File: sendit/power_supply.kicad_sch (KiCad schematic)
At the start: 1 part, among them U9 TPS61040DBV

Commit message: bigger update
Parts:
- added C22: C_Small, symbol Device:C_Small
- added C23: 22pF, symbol Device:C_Small
- added C24: 1uF, symbol Device:C_Small
- added D17: MBR0530, Diode_SMD:D_SOD-123, symbol Diode:MBR0530
- added L1: 10uH, symbol Device:L
- added R68: 1.87M, symbol Device:R_Small_US
- added R69: 100k, symbol Device:R_Small_US
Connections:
- net at U9.1 (SW): now also D17.2 (A), L1.2
- net GND: now reaches U9.2 (GND)
- net GND: now also C22.2, C24.2, R69.2
- net at U9.3 (FB): now also C23.2, R68.2, R69.1
- net +5V: now reaches U9.4 (EN)
- net +5V: now also U9.5 (VIN), C22.1, L1.1
- new net +24V: C23.1, C24.1, D17.1 (K), R68.1

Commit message: layout work.
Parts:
- C10: renamed from C22; value C_Small -> 10uF; footprint (none) -> Capacitor_SMD:C_0603_1608Metric
- C11: renamed from C23; footprint (none) -> Capacitor_SMD:C_0603_1608Metric
- C12: renamed from C24; footprint (none) -> Capacitor_SMD:C_1206_3216Metric
- L1: footprint (none) -> Inductor_SMD:L_Ferrocore_DLG-0403; LCSC (none) -> C2929419
- R43: renamed from R68; footprint (none) -> Resistor_SMD:R_0603_1608Metric
- R44: renamed from R69; footprint (none) -> Resistor_SMD:R_0603_1608Metric
- renumbered D17 to D6, U9 to U4
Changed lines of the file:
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@@
 		(dnp no)
 		(fields_autoplaced yes)
-		(property "Reference" "#PWR0113"
+		(property "Reference" "#PWR067"
 			(at 129.54 121.92 0)
 			(effects
@@
 			(project "sendit"
 				(path "/a355e4d0-2918-44fc-be8d-2503b84c6d6c/336de2d2-126c-456c-9b27-fa88f8fd80ba"
-					(reference "#PWR0113")
+					(reference "#PWR067")
 					(unit 1)
 				)
@@
 		(dnp no)
 		(fields_autoplaced yes)
-		(property "Reference" "C24"
+		(property "Reference" "C12"
 			(at 182.88 90.1762 0)
 			(effects
@@
 			)
 		)
-		(property "Footprint" ""
+		(property "Footprint" "Capacitor_SMD:C_1206_3216Metric"
 			(at 180.34 91.44 0)
 			(effects
@@
 			(project "sendit"
 				(path "/a355e4d0-2918-44fc-be8d-2503b84c6d6c/336de2d2-126c-456c-9b27-fa88f8fd80ba"
-					(reference "C24")
+					(reference "C12")
 					(unit 1)
 				)
@@
 		(dnp no)
 		(fields_autoplaced yes)
-		(property "Reference" "R69"
+		(property "Reference" "R44"
 			(at 157.48 102.8699 0)
 			(effects
@@
 			)
 		)
-		(property "Footprint" ""
+		(property "Footprint" "Resistor_SMD:R_0603_1608Metric"
 			(at 154.94 104.14 0)
 			(effects
@@
 			(project "sendit"
 				(path "/a355e4d0-2918-44fc-be8d-2503b84c6d6c/336de2d2-126c-456c-9b27-fa88f8fd80ba"
-					(reference "R69")
+					(reference "R44")
 					(unit 1)
 				)
@@
 		(dnp no)
 		(fields_autoplaced yes)
-		(property "Reference" "U9"
+		(property "Reference" "U4"
 			(at 129.54 87.63 0)
 			(effects
@@
 			(project ""
 				(path "/a355e4d0-2918-44fc-be8d-2503b84c6d6c/336de2d2-126c-456c-9b27-fa88f8fd80ba"
-					(reference "U9")
+					(reference "U4")
 					(unit 1)
 				)
@@
 		(dnp no)
 		(fields_autoplaced yes)
-		(property "Reference" "C23"
+		(property "Reference" "C11"
 			(at 170.18 90.1762 0)
 			(effects
@@
 			)
 		)
-		(property "Footprint" ""
+		(property "Footprint" "Capacitor_SMD:C_0603_1608Metric"
 			(at 167.64 91.44 0)
 			(effects
@@
 			(project "sendit"
 				(path "/a355e4d0-2918-44fc-be8d-2503b84c6d6c/336de2d2-126c-456c-9b27-fa88f8fd80ba"
-					(reference "C23")
+					(reference "C11")
 					(unit 1)
 				)
@@
 			)
 		)
-		(property "Footprint" ""
+		(property "Footprint" "Inductor_SMD:L_Ferrocore_DLG-0403"
 			(at 129.54 82.55 0)
 			(effects
@@
 			)
 		)
+		(property "LCSC" "C2929419"
+			(at 129.54 82.55 90)
+			(effects
+				(font
+					(size 1.27 1.27)
+				)
+				(hide yes)
+			)
+		)
 		(pin "1"
 		)
@@
 		(dnp no)
 		(fields_autoplaced yes)
-		(property "Reference" "R68"
+		(property "Reference" "R43"
 			(at 157.48 90.1699 0)
 			(effects
@@
 			)
 		)
-		(property "Footprint" ""
+		(property "Footprint" "Resistor_SMD:R_0603_1608Metric"
 			(at 154.94 91.44 0)
 			(effects
@@
 			(project ""
 				(path "/a355e4d0-2918-44fc-be8d-2503b84c6d6c/336de2d2-126c-456c-9b27-fa88f8fd80ba"
-					(reference "R68")
+					(reference "R43")
 					(unit 1)
 				)
@@
 		(dnp no)
 		(fields_autoplaced yes)
-		(property "Reference" "C22"
+		(property "Reference" "C10"
 			(at 105.41 100.3362 0)
 			(effects
@@
 			)
 		)
-		(property "Value" "C_Small"
+		(property "Value" "10uF"
 			(at 105.41 102.8762 0)
 			(effects
@@
 			)
 		)
-		(property "Footprint" ""
+		(property "Footprint" "Capacitor_SMD:C_0603_1608Metric"
 			(at 102.87 101.6 0)
 			(effects
@@
 			(project ""
 				(path "/a355e4d0-2918-44fc-be8d-2503b84c6d6c/336de2d2-126c-456c-9b27-fa88f8fd80ba"
-					(reference "C22")
+					(reference "C10")
 					(unit 1)
 				)
@@
 		(dnp no)
 		(fields_autoplaced yes)
-		(property "Reference" "D17"
+		(property "Reference" "D6"
 			(at 147.6375 76.2 0)
 			(effects
@@
 			(project ""
 				(path "/a355e4d0-2918-44fc-be8d-2503b84c6d6c/336de2d2-126c-456c-9b27-fa88f8fd80ba"
-					(reference "D17")
+					(reference "D6")
 					(unit 1)
 				)
@@
 		(dnp no)
 		(fields_autoplaced yes)
-		(property "Reference" "#PWR0112"
+		(property "Reference" "#PWR068"
 			(at 180.34 83.82 0)
 			(effects
@@
 			(project "sendit"
 				(path "/a355e4d0-2918-44fc-be8d-2503b84c6d6c/336de2d2-126c-456c-9b27-fa88f8fd80ba"
-					(reference "#PWR0112")
+					(reference "#PWR068")
 					(unit 1)
 				)
@@
 		(dnp no)
 		(fields_autoplaced yes)
-		(property "Reference" "#PWR0111"
+		(property "Reference" "#PWR066"
 			(at 102.87 83.82 0)
 			(effects
@@
 			(project "sendit"
 				(path "/a355e4d0-2918-44fc-be8d-2503b84c6d6c/336de2d2-126c-456c-9b27-fa88f8fd80ba"
-					(reference "#PWR0111")
-					(unit 1)
-				)
+					(reference "#PWR066")
+					(unit 1)
+				)

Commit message: updated footprints and lcsc numbers.
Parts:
- C10: LCSC (none) -> C19702
- C11: LCSC (none) -> C105620
- C12: footprint Capacitor_SMD:C_1206_3216Metric -> Capacitor_SMD:C_0603_1608Metric; LCSC (none) -> C15849
- D6: LCSC (none) -> C82046
- U4: LCSC (none) -> C7722
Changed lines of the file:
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@@
 			)
 		)
-		(property "Footprint" "Capacitor_SMD:C_1206_3216Metric"
+		(property "Footprint" "Capacitor_SMD:C_0603_1608Metric"
 			(at 180.34 91.44 0)
 			(effects
@@
 			)
 		)
+		(property "LCSC" "C15849"
+			(at 180.34 91.44 0)
+			(effects
+				(font
+					(size 1.27 1.27)
+				)
+				(hide yes)
+			)
+		)
 		(pin "1"
 		)
@@
 			)
 		)
+		(property "LCSC" "C7722"
+			(at 129.54 97.79 0)
+			(effects
+				(font
+					(size 1.27 1.27)
+				)
+				(hide yes)
+			)
+		)
 		(pin "1"
 		)
@@
 			)
 		)
+		(property "LCSC" "C105620"
+			(at 167.64 91.44 0)
+			(effects
+				(font
+					(size 1.27 1.27)
+				)
+				(hide yes)
+			)
+		)
 		(pin "1"
 		)
@@
 			)
 		)
+		(property "LCSC" "C19702"
+			(at 102.87 101.6 0)
+			(effects
+				(font
+					(size 1.27 1.27)
+				)
+				(hide yes)
+			)
+		)
 		(pin "1"
 		)
@@
 			(at 147.32 82.55 0)
 			(effects
+				(font
+					(size 1.27 1.27)
+				)
+				(hide yes)
+			)
+		)
+		(property "LCSC" "C82046"
+			(at 147.32 82.55 0)
+			(effects

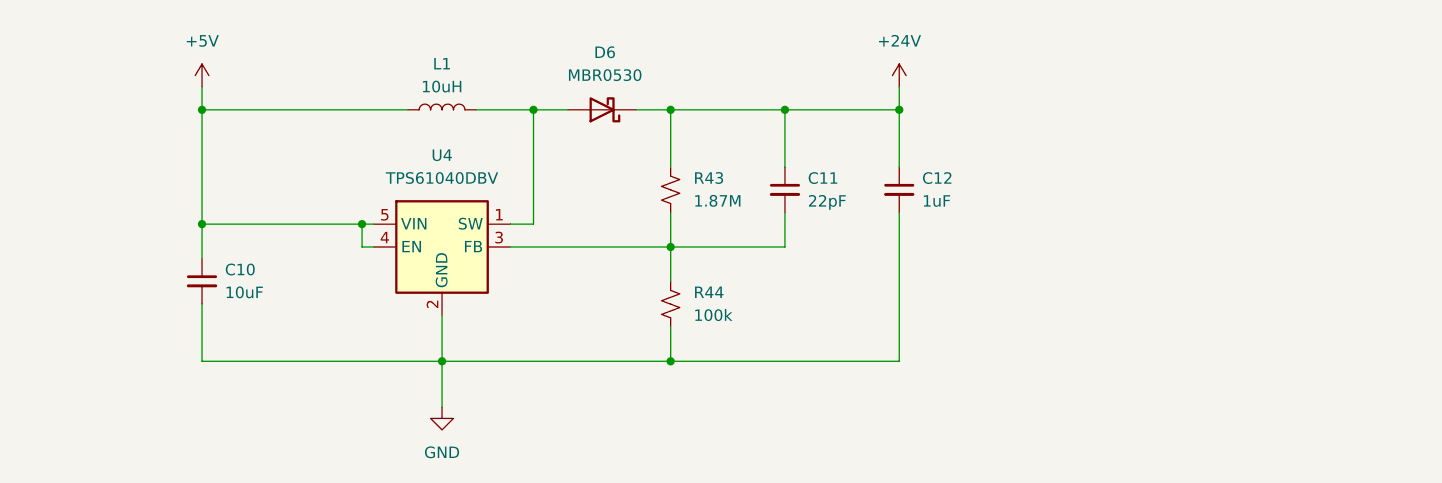
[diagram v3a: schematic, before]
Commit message: added fuses, 24v filters, and indicator leds.
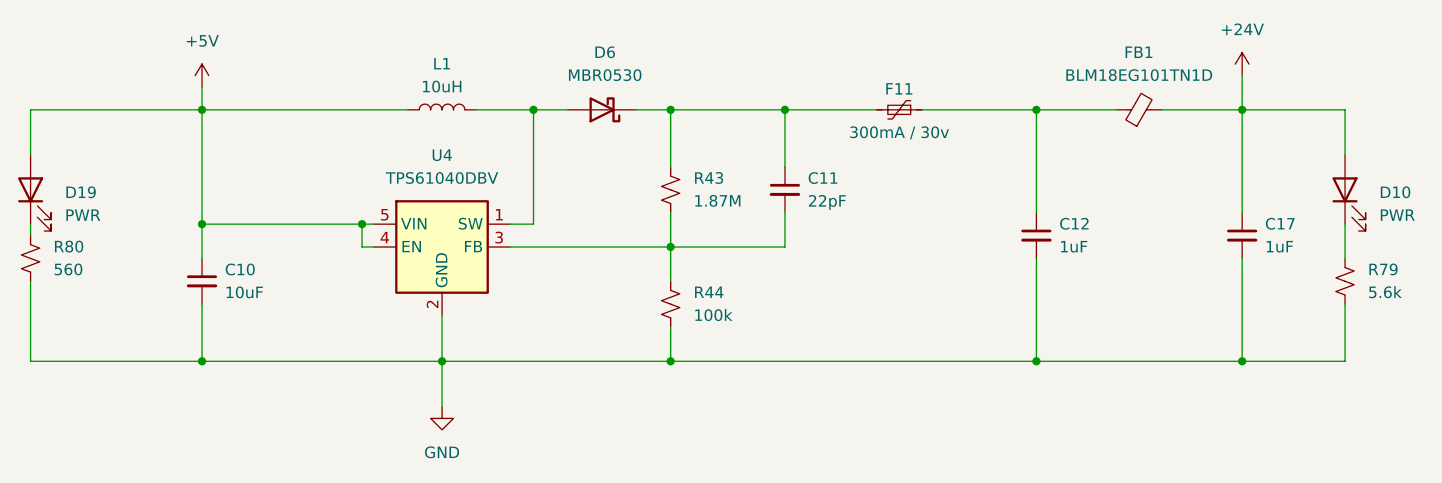
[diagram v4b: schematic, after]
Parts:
- added C17: 1uF, Capacitor_SMD:C_0603_1608Metric, symbol Device:C_Small
- added D10, D19: PWR, LED_SMD:LED_0603_1608Metric, symbol Device:LED
- added F11: 300mA / 30v, Fuse:Fuse_0805_2012Metric, symbol Device:Polyfuse_Small
- added FB1: BLM18EG101TN1D, Inductor_SMD:L_0603_1608Metric, symbol Device:FerriteBead_Small
- added R79: 5.6k, Resistor_SMD:R_0603_1608Metric, symbol Device:R_Small_US
- added R80: 560, Resistor_SMD:R_0603_1608Metric, symbol Device:R_Small_US
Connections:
- net +24V: now also C17.1, D10.2 (A), FB1.2; no longer C11.1, C12.1, D6.1 (K), R43.1
- net +5V: now also D19.2 (A)
- net GND: now also C17.2, R79.2, R80.2
- new net: D10.1 (K), R79.1
- new net: C12.1, F11.1, FB1.1
- new net: D19.1 (K), R80.1
- new net: C11.1, D6.1 (K), F11.2, R43.1
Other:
- moved on the sheet: C12

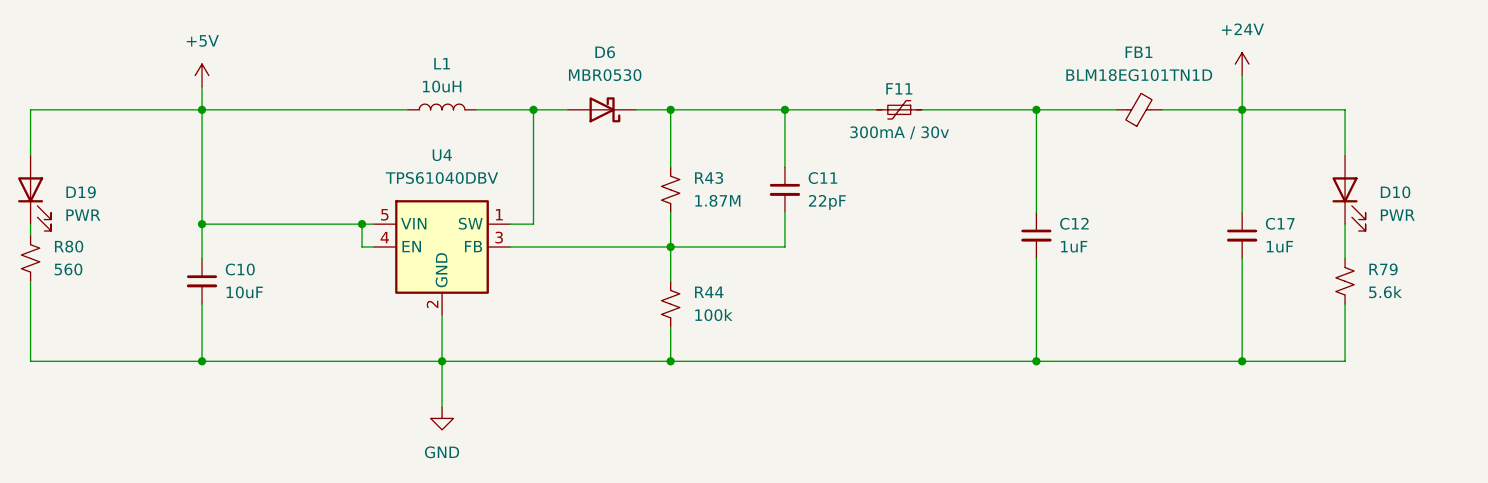
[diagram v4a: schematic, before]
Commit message: test run of jlcpcb upload looks good.
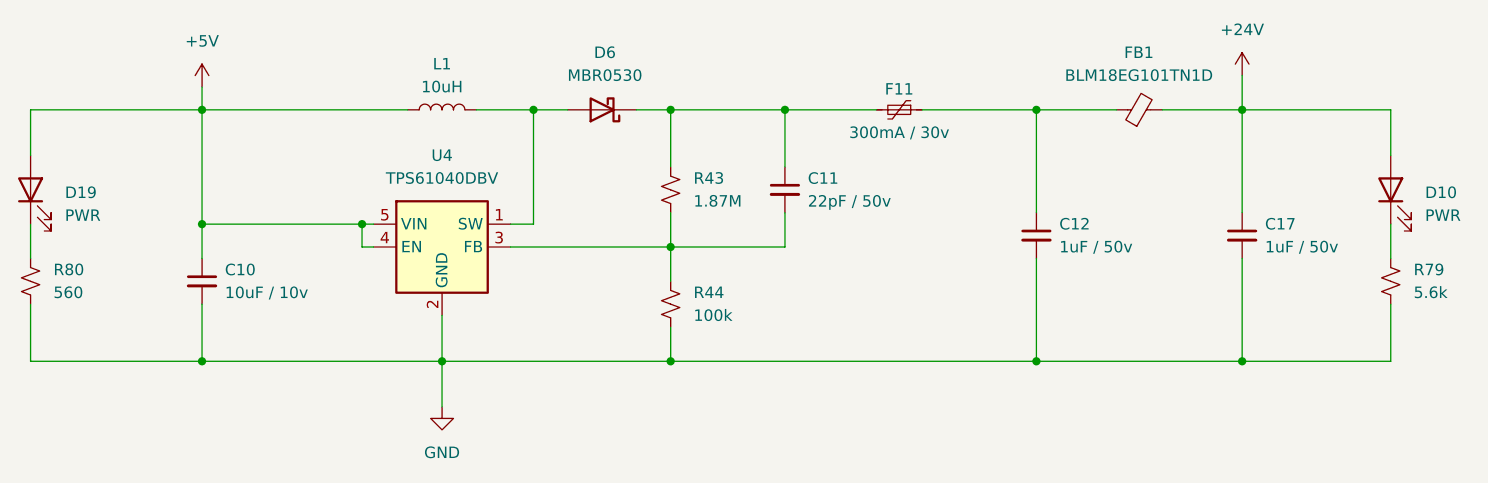
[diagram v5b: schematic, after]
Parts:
- C10: value 10uF -> 10uF / 10v
- C11: value 22pF -> 22pF / 50v; LCSC C105620 -> C1653
- C12, C17: value 1uF -> 1uF / 50v
- D10, D19: LCSC (none) -> C94869
- R43: LCSC (none) -> C61679
- R44: LCSC (none) -> C25803
- R79: LCSC (none) -> C23189
- R80: LCSC (none) -> C23204
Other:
- moved on the sheet: D10, R79, R80
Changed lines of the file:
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@@
 	(wire
 		(pts
-			(xy 229.87 110.49) (xy 229.87 104.14)
+			(xy 234.95 110.49) (xy 234.95 104.14)
 		)
 		(stroke
@@
 	(wire
 		(pts
-			(xy 83.82 101.6) (xy 83.82 110.49)
+			(xy 83.82 104.14) (xy 83.82 110.49)
 		)
 		(stroke
@@
 	(wire
 		(pts
-			(xy 229.87 82.55) (xy 229.87 87.63)
-		)
-		(stroke
-			(width 0)
-			(type default)
-		)
-	)
-	(wire
-		(pts
-			(xy 229.87 95.25) (xy 229.87 99.06)
-		)
-		(stroke
-			(width 0)
-			(type default)
-		)
-	)
-	(wire
-		(pts
-			(xy 218.44 110.49) (xy 229.87 110.49)
+			(xy 234.95 82.55) (xy 234.95 87.63)
+		)
+		(stroke
+			(width 0)
+			(type default)
+		)
+	)
+	(wire
+		(pts
+			(xy 234.95 95.25) (xy 234.95 99.06)
+		)
+		(stroke
+			(width 0)
+			(type default)
+		)
+	)
+	(wire
+		(pts
+			(xy 218.44 110.49) (xy 234.95 110.49)
 		)
 		(stroke
@@
 	(wire
 		(pts
-			(xy 218.44 82.55) (xy 229.87 82.55)
+			(xy 218.44 82.55) (xy 234.95 82.55)
 		)
 		(stroke
@@
 	(wire
 		(pts
-			(xy 83.82 95.25) (xy 83.82 96.52)
+			(xy 83.82 95.25) (xy 83.82 99.06)
 		)
 		(stroke
@@
 			)
 		)
-		(property "Value" "1uF"
+		(property "Value" "1uF / 50v"
 			(at 220.98 97.7962 0)
 			(effects
@@
 	(symbol
 		(lib_id "Device:LED")
-		(at 229.87 91.44 90)
+		(at 234.95 91.44 90)
 		(unit 1)
 		(exclude_from_sim no)
@@
 		(fields_autoplaced yes)
 		(property "Reference" "D10"
-			(at 233.68 91.7574 90)
+			(at 238.76 91.7574 90)
 			(effects
 				(font
@@
 		)
 		(property "Value" "PWR"
-			(at 233.68 94.2974 90)
+			(at 238.76 94.2974 90)
 			(effects
 				(font
@@
 		)
 		(property "Footprint" "LED_SMD:LED_0603_1608Metric"
-			(at 229.87 91.44 0)
+			(at 234.95 91.44 0)
 			(effects
 				(font
@@
 		)
 		(property "Datasheet" "~"
-			(at 229.87 91.44 0)
+			(at 234.95 91.44 0)
 			(effects
 				(font
@@
 		)
 		(property "Description" "Light emitting diode"
-			(at 229.87 91.44 0)
+			(at 234.95 91.44 0)
 			(effects
 				(font
@@
 		)
 		(property "Sim.Pins" "1=K 2=A"
-			(at 229.87 91.44 0)
+			(at 234.95 91.44 0)
+			(effects
+				(font
+					(size 1.27 1.27)
+				)
+				(hide yes)
+			)
+		)
+		(property "LCSC" "C94869"
+			(at 234.95 91.44 90)
 			(effects
 				(font
@@
 			)
 		)
-		(property "Value" "1uF"
+		(property "Value" "1uF / 50v"
 			(at 198.12 97.7962 0)
 			(effects
@@
 			)
 		)
+		(property "LCSC" "C25803"
+			(at 154.94 104.14 0)
+			(effects
+				(font
+					(size 1.27 1.27)
+				)
+				(hide yes)
+			)
+		)
 		(pin "1"
 		)
@@
 	(symbol
 		(lib_id "Device:R_Small_US")
-		(at 83.82 99.06 0)
+		(at 83.82 101.6 0)
 		(unit 1)
 		(exclude_from_sim no)
@@
 		(fields_autoplaced yes)
 		(property "Reference" "R80"
-			(at 86.36 97.7899 0)
+			(at 86.36 100.3299 0)
 			(effects
 				(font
@@
 		)
 		(property "Value" "560"
-			(at 86.36 100.3299 0)
+			(at 86.36 102.8699 0)
 			(effects
 				(font
@@
 		)
 		(property "Footprint" "Resistor_SMD:R_0603_1608Metric"
-			(at 83.82 99.06 0)
+			(at 83.82 101.6 0)
 			(effects
 				(font
@@
 		)
 		(property "Datasheet" "~"
-			(at 83.82 99.06 0)
+			(at 83.82 101.6 0)
 			(effects
 				(font
@@
 		)
 		(property "Description" "Resistor, small US symbol"
-			(at 83.82 99.06 0)
+			(at 83.82 101.6 0)
+			(effects
+				(font
+					(size 1.27 1.27)
+				)
+				(hide yes)
+			)
+		)
+		(property "LCSC" "C23204"
+			(at 83.82 101.6 0)
 			(effects
 				(font
@@
 			)
 		)
-		(property "Value" "22pF"
+		(property "Value" "22pF / 50v"
 			(at 170.18 92.7162 0)
 			(effects
@@
 			)
 		)
-		(property "LCSC" "C105620"
+		(property "LCSC" "C1653"
 			(at 167.64 91.44 0)
 			(effects
@@
 			)
 		)
+		(property "LCSC" "C61679"
+			(at 154.94 91.44 0)
+			(effects
+				(font
+					(size 1.27 1.27)
+				)
+				(hide yes)
+			)
+		)
 		(pin "1"
 		)
@@
 			)
 		)
-		(property "Value" "10uF"
+		(property "Value" "10uF / 10v"
 			(at 105.41 102.8762 0)
 			(effects
@@
 			)
 		)
+		(property "LCSC" "C94869"
+			(at 83.82 91.44 90)
+			(effects
+				(font
+					(size 1.27 1.27)
+				)
+				(hide yes)
+			)
+		)
 		(pin "1"
 		)
@@
 	(symbol
 		(lib_id "Device:R_Small_US")
-		(at 229.87 101.6 0)
+		(at 234.95 101.6 0)
 		(unit 1)
 		(exclude_from_sim no)
@@
 		(fields_autoplaced yes)
 		(property "Reference" "R79"
-			(at 232.41 100.3299 0)
+			(at 237.49 100.3299 0)
 			(effects
 				(font
@@
 		)
 		(property "Value" "5.6k"
-			(at 232.41 102.8699 0)
+			(at 237.49 102.8699 0)
 			(effects
 				(font
@@
 		)
 		(property "Footprint" "Resistor_SMD:R_0603_1608Metric"
-			(at 229.87 101.6 0)
+			(at 234.95 101.6 0)
 			(effects
 				(font
@@
 		)
 		(property "Datasheet" "~"
-			(at 229.87 101.6 0)
+			(at 234.95 101.6 0)
 			(effects
 				(font
@@
 		)
 		(property "Description" "Resistor, small US symbol"
-			(at 229.87 101.6 0)
-			(effects
-				(font
+			(at 234.95 101.6 0)
+			(effects
+				(font
+					(size 1.27 1.27)
+				)
+				(hide yes)
+			)
+		)
+		(property "LCSC" "C23189"
+			(at 234.95 101.6 0)
+			(effects
+				(font

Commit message: changed inductor on 24v circuit, cleaned up board a bit.
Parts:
- L1: footprint Inductor_SMD:L_Ferrocore_DLG-0403 -> Inductor_SMD:L_APV_ANR252012; LCSC C2929419 -> C5832376
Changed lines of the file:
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@@
 			)
 		)
-		(property "Footprint" "Inductor_SMD:L_Ferrocore_DLG-0403"
+		(property "Footprint" "Inductor_SMD:L_APV_ANR252012"
 			(at 129.54 82.55 0)
 			(effects
@@
 			)
 		)
-		(property "LCSC" "C2929419"
+		(property "LCSC" "C5832376"
 			(at 129.54 82.55 90)
 			(effects

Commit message: Rev-A ready for production
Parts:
- added D11: PWR, LED_SMD:LED_0603_1608Metric, symbol Device:LED
- added R81: 220, Resistor_SMD:R_0603_1608Metric, symbol Device:R_Small_US
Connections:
- net GND: now also R81.2
- new net: D11.1 (K), R81.1
- new net +3.3V: D11.2 (A)

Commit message: big schematic rework for Rev B
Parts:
- added C31, C37, C40, C43: 1uF, Capacitor_SMD:C_0603_1608Metric, symbol Device:C_Small
- added C32, C34, C38, C42: 100nF, Capacitor_SMD:C_0603_1608Metric, symbol Device:C_Small
- added C33: 1nF, Capacitor_SMD:C_0402_1005Metric, symbol Device:C_Small
- added C36: 10uF, Capacitor_SMD:C_0805_2012Metric, symbol Device:C_Small
- added D11: PESD3V3L1BA, Diode_SMD:D_SOD-323, symbol Device:D_TVS
- added D9: B5819W, Diode_SMD:D_SOD-123, symbol Device:D_Schottky
- added FB3: BLM18AG121SN1D, Inductor_SMD:L_0603_1608Metric, symbol Device:FerriteBead_Small
- added R57, R58, R61, R62: 0R, Resistor_SMD:R_0603_1608Metric, symbol Device:R_Small_US
- added TP11: ~, TestPoint:TestPoint_THTPad_D2.0mm_Drill1.0mm, symbol Connector:TestPoint
- added TP12: TestPoint, TestPoint:TestPoint_THTPad_D2.0mm_Drill1.0mm, symbol Connector:TestPoint
- added U7: TPS7A2033PDBVR, Package_TO_SOT_SMD:SOT-23-5, symbol yarrboard:TPS7A2033PDBVR
- added U9: REF35330QDBVR, Package_TO_SOT_SMD:SOT-23-6, symbol Reference_Voltage:REF35330QDBVR
- R55: renamed from R81; value 220 -> 5.1k
- R56: renamed from R80; value 560 -> 10k
- R63: renamed from R79; value 5.6k -> 100k
- renumbered C10 to C35, C11 to C39, C12 to C41, C17 to C44, D19 to D10, D6 to D12, D10 to D13, D11 to D8, F11 to F6, FB1 to FB4, R43 to R59, R44 to R60, U4 to U8
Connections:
- net +3.3V: now also R58.2
- net +5V: now also C31.1, C37.1, C38.1, D9.1 (K), FB3.1, U9.3 (EN), U9.4 (VIN)
- net GND: now also C31.2, C32.2, C33.2, C34.2, C36.2, C37.2, C38.2, C40.2, C42.2, C43.2, D11.1 (A1), U7.2 (GND), U9.1 (GND), U9.2 (GND)
- new net: C33.1, C34.1, C36.1, D11.2 (A2), D9.2 (A), R57.1, TP11.1, U7.5 (OUT)
- new net: C32.1, FB3.2, U7.1 (IN), U7.3 (EN)
- new net: C42.1, C43.1, R61.1, TP12.1, U9.6 (VREF)
- new net: C40.1, U9.5 (NR)
- new net +3.3VADC: R57.2, R58.1, R62.2
- new net REF_3V3: R61.2, R62.1
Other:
- note added: "ADC Power Supply"
- note added: "ADC Reference Voltage Circuit"
- moved on the sheet: C35, C39, C41, C44, D10, D12, D13, D8, F6, FB4, L1, R55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
